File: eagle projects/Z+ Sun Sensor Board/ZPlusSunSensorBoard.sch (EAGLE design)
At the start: 50 parts, among them U2 ADS7841E_2K5, U4 LM20BIM7X_NOPB, U6 TLV9051IDCKR, U8 TLV9051IDCKR, U9 TLV9051IDCKR

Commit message: Rev B almost ready
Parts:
- removed A1: SUN_SENSOR_MOUNT, my_library:SUN_SENSOR_MOUNT
- removed C25, C28, C30: 4.7u, rcl:C-EUC0805
- removed C26, C29, C31: 0.1u, resistor:C-EUC0402
- removed C27, C32, C33: 0.022u, resistor:C-EUC0402
- removed J4, J5, J6: (no value), my_library:TRM_BLK_1X2
- removed R13, R19, R7: 3.74k, resistor:R-US_R0402
- removed R14, R8: 280R, resistor:R-US_R0402
- removed R15: 13.7k, resistor:R-US_R0402
- removed TP3, TP6, TP8: TESTPOINT, my_library:TESTPOINT
- removed U6, U9: TLV9051IDCKR, my_library:TLV9051IDCKR
- added C1, C17, C7: 4.7u, rcl:C-EUC0805
- added C18, C2, C8: 0.1u, resistor:C-EUC0402
- added C23, C3, C9: 0.022u, resistor:C-EUC0402
- added R10, R18: 13.7k, resistor:R-US_R0402
- added R11, R21, R5: 3.74k, resistor:R-US_R0402
- added R17: 280R, resistor:R-US_R0402
- added TP10, TP12, TP7: TESTPOINT, my_library:TESTPOINT
- added U$1: SSR_MOUNT_03, my_library:SSR_MOUNT_03
- added U1, U5: TSV991AILT, my_library:TSV991AILT
- R9: value 13.7k -> 280R
- U8: value TLV9051IDCKR -> TSV991AILT; device my_library:TLV9051IDCKR -> my_library:TSV991AILT
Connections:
- removed net N$13: R14.2, R15.1, U9.+
- removed net N$6: R1.2, R3.1, U6.+
- removed net N$9: R8.2, R9.1, U8.+
- new net N$11: C9.1, R11.1, U$1G$2.C2, U5.IN-
- new net N$14: R10.1, R9.2, U5.IN+
- new net N$20: R17.2, R18.1, U8.IN+
- net +3V3: now also C1.1, C17.1, C18.1, C2.1, C7.1, C8.1, R10.2, R18.2, U1.VCC, U5.VCC, U8.VCC; no longer C25.1, C26.1, C28.1, C29.1, C30.1, C31.1, R15.2, R9.2, U6.V+, U8.V+, U9.V+
- net 0_DEGREES: now also C3.2, R5.2, TP7.TP, U1.OUT; no longer C27.2, R7.2, TP3.TP, U6.OUT
- net 120_DEGREES: now also C9.2, R11.2, TP10.TP, U5.OUT; no longer C32.2, R13.2, TP6.TP, U8.OUT
- net 240_DEGREES: now also C23.2, R21.2, TP12.TP, U8.OUT; no longer C33.2, R19.2, TP8.TP, U9.OUT
- net GND: now also C1.2, C17.2, C18.2, C2.2, C7.2, C8.2, R17.1, R9.1, U$1G$2.A1, U$1G$2.A2, U$1G$2.A3, U1.VSS, U5.VSS, U8.VSS; no longer C25.2, C26.2, C28.2, C29.2, C30.2, C31.2, J4.1, J5.1, J6.1, R14.1, R8.1, U6.V-, U8.V-, U9.V-
- net N$12: now also C23.1, R21.1, U$1G$2.C3, U8.IN-; no longer C33.1, J4.2, R19.1, U9.-
- net N$3: now also C3.1, R5.1, U$1G$2.C1, U1.IN-; no longer C27.1, J6.2, R7.1, U6.-
- net N$8: now also R1.2, R3.1, U1.IN+; no longer C32.1, J5.2, R13.1, U8.-
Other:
- moved on the sheet: R1, R3, R9

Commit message: I thinks its done
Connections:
- net GND: now also H1.MOUNT, H2.MOUNT, H3.MOUNT, H4.MOUNT
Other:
- note added: "B"
- note removed: "A"
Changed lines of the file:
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@@
 <schematic xreflabel="%F%N" xrefpart="/%S.%C%R">
 <attributes>
-<attribute name="DESIGNER" value="T. Christison"/>
+<attribute name="DESIGNER" value="Thomas Christison"/>
+<attribute name="REV" value="B"/>
+<attribute name="REVIEWER" value="ADCS Electrical"/>
 </attributes>
 <variantdefs>
@@
 <part name="C12" library="rcl" library_urn="urn:adsk.eagle:library:334" deviceset="C-EU" device="C0402" package3d_urn="urn:adsk.eagle:package:23626/2" value="0.1u"/>
 <part name="SUPPLY24" library="supply2" library_urn="urn:adsk.eagle:library:372" deviceset="GND" device=""/>
-<part name="U2" library="my_library" library_urn="urn:adsk.eagle:library:22876504" deviceset="ADS7841E_2K5" device="" package3d_urn="urn:adsk.eagle:package:23087509/5"/>
+<part name="U2" library="my_library" library_urn="urn:adsk.eagle:library:22876504" deviceset="ADS7841E_2K5" device="" package3d_urn="urn:adsk.eagle:package:23087509/6"/>
 <part name="C14" library="resistor" library_urn="urn:adsk.eagle:library:348" deviceset="C-EU" device="C0402" package3d_urn="urn:adsk.eagle:package:23626/2" value="1u"/>
 <part name="C15" library="resistor" library_urn="urn:adsk.eagle:library:348" deviceset="C-EU" device="C0402" package3d_urn="urn:adsk.eagle:package:23626/2" value="0.1u"/>
@@
 <attribute name="DESIGNER" value=""/>
 <attribute name="REV#" value=""/>
+<attribute name="REVIEWER" value=""/>
 </part>
 <part name="R4" library="resistor" library_urn="urn:adsk.eagle:library:348" deviceset="R-US_" device="R0402" package3d_urn="urn:adsk.eagle:package:26058/2" value="5.1M"/>
 <part name="SUPPLY3" library="supply2" library_urn="urn:adsk.eagle:library:372" deviceset="GND" device=""/>
-<part name="U$1" library="my_library" library_urn="urn:adsk.eagle:library:22876504" deviceset="SSR_MOUNT_03" device="" package3d_urn="urn:adsk.eagle:package:29580098/1"/>
+<part name="U$1" library="my_library" library_urn="urn:adsk.eagle:library:22876504" deviceset="SSR_MOUNT_03" device="" package3d_urn="urn:adsk.eagle:package:29580098/1" override_package3d_urn="urn:adsk.eagle:package:30064049/2" override_package_urn="urn:adsk.eagle:footprint:29580096/1"/>
 <part name="SUPPLY6" library="supply2" library_urn="urn:adsk.eagle:library:372" deviceset="GND" device=""/>
 <part name="C1" library="rcl" library_urn="urn:adsk.eagle:library:334" deviceset="C-EU" device="C0805" package3d_urn="urn:adsk.eagle:package:23617/2" value="4.7u"/>
@@
 <part name="+3V11" library="supply1" library_urn="urn:adsk.eagle:library:371" deviceset="+3V3" device=""/>
 <part name="U8" library="my_library" library_urn="urn:adsk.eagle:library:22876504" deviceset="TSV991AILT" device="" package3d_urn="urn:adsk.eagle:package:24426275/2"/>
+<part name="SUPPLY13" library="supply2" library_urn="urn:adsk.eagle:library:372" deviceset="GND" device=""/>
+<part name="SUPPLY14" library="supply2" library_urn="urn:adsk.eagle:library:372" deviceset="GND" device=""/>
+<part name="SUPPLY15" library="supply2" library_urn="urn:adsk.eagle:library:372" deviceset="GND" device=""/>
+<part name="SUPPLY16" library="supply2" library_urn="urn:adsk.eagle:library:372" deviceset="GND" device=""/>
 </parts>
 <sheets>
 <sheet>
 <plain>
-<text x="262.128" y="7.112" size="2.54" layer="94">A</text>
+<text x="262.128" y="7.112" size="2.54" layer="94">B</text>
 <text x="190.754" y="11.43" size="2.54" layer="94">T. Christison</text>
 </plain>
@@
 <attribute name="REV#" x="261.62" y="7.62" size="2.54" layer="94"/>
 <attribute name="DESIGNER" x="196.85" y="11.43" size="2.54" layer="94"/>
+<attribute name="REVIEWER" x="196.85" y="6.35" size="2.54" layer="94"/>
 </instance>
 <instance part="R4" gate="G$1" x="233.68" y="93.98" smashed="yes" rot="R90">
@@
 <attribute name="NAME" x="99.06" y="53.34" size="1.778" layer="95"/>
 <attribute name="VALUE" x="99.06" y="50.8" size="1.778" layer="96"/>
+</instance>
+<instance part="SUPPLY13" gate="GND" x="10.16" y="7.62" smashed="yes">
+<attribute name="VALUE" x="8.255" y="4.445" size="1.778" layer="96"/>
+</instance>
+<instance part="SUPPLY14" gate="GND" x="48.26" y="7.62" smashed="yes">
+<attribute name="VALUE" x="46.355" y="4.445" size="1.778" layer="96"/>
+</instance>
+<instance part="SUPPLY15" gate="GND" x="88.9" y="7.62" smashed="yes">
+<attribute name="VALUE" x="86.995" y="4.445" size="1.778" layer="96"/>
+</instance>
+<instance part="SUPPLY16" gate="GND" x="129.54" y="7.62" smashed="yes">
+<attribute name="VALUE" x="127.635" y="4.445" size="1.778" layer="96"/>
 </instance>
 </instances>
@@
 <pinref part="SUPPLY36" gate="GND" pin="GND"/>
 <pinref part="U8" gate="G$1" pin="VSS"/>
+</segment>
+<segment>
+<pinref part="SUPPLY13" gate="GND" pin="GND"/>
+<wire x1="10.16" y1="10.16" x2="10.16" y2="12.7" width="0.1524" layer="91"/>
+<pinref part="H1" gate="G$1" pin="MOUNT"/>
+<wire x1="10.16" y1="12.7" x2="12.7" y2="12.7" width="0.1524" layer="91"/>
+</segment>
+<segment>
+<pinref part="SUPPLY14" gate="GND" pin="GND"/>
+<wire x1="48.26" y1="10.16" x2="48.26" y2="12.7" width="0.1524" layer="91"/>
+<pinref part="H2" gate="G$1" pin="MOUNT"/>
+<wire x1="48.26" y1="12.7" x2="50.8" y2="12.7" width="0.1524" layer="91"/>
+</segment>
+<segment>
+<pinref part="SUPPLY15" gate="GND" pin="GND"/>
+<wire x1="88.9" y1="10.16" x2="88.9" y2="12.7" width="0.1524" layer="91"/>
+<pinref part="H3" gate="G$1" pin="MOUNT"/>
+<wire x1="88.9" y1="12.7" x2="91.44" y2="12.7" width="0.1524" layer="91"/>
+</segment>
+<segment>
+<pinref part="SUPPLY16" gate="GND" pin="GND"/>
+<wire x1="129.54" y1="10.16" x2="129.54" y2="12.7" width="0.1524" layer="91"/>
+<pinref part="H4" gate="G$1" pin="MOUNT"/>
+<wire x1="129.54" y1="12.7" x2="132.08" y2="12.7" width="0.1524" layer="91"/>
 </segment>
 </net>
@@
 will not be understood (or retained) with this version.
 </note>
+<note version="9.4" severity="warning">
+Since Version 9.4, EAGLE supports the overriding of 3D packages
+in schematics and board files. Those overridden 3d packages
+will not be understood (or retained) with this version.
+</note>

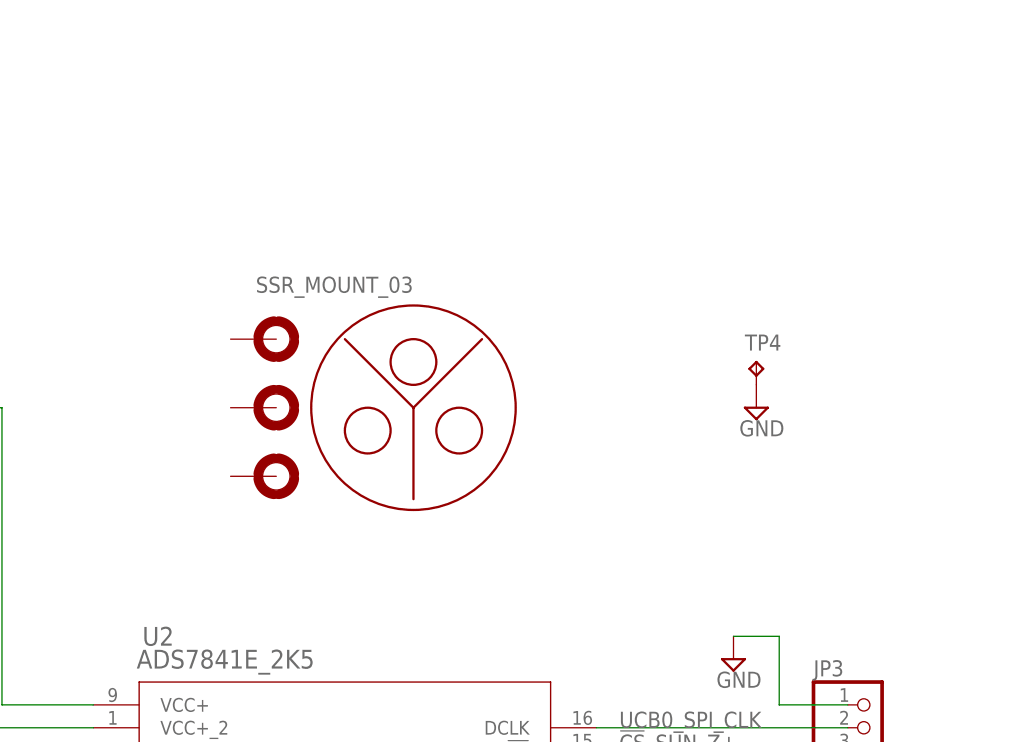
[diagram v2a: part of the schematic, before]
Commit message: Brandon added burn resistor components
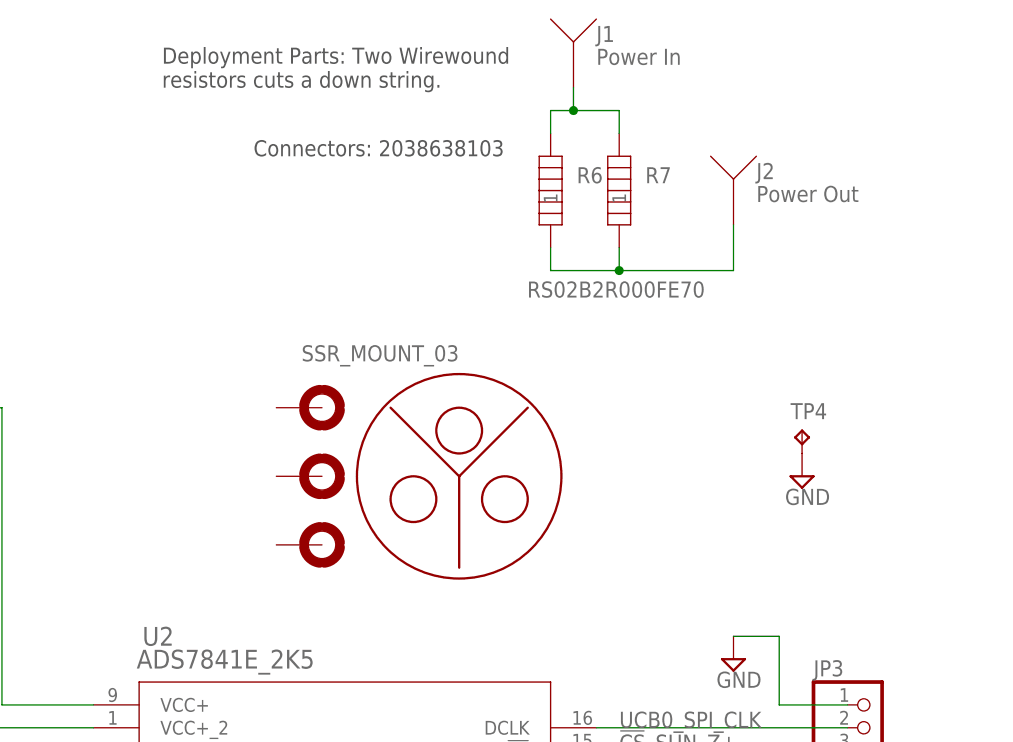
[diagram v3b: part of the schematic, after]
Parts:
- added J1: Power In, PDUv1:2038638103
- added J2: Power Out, PDUv1:2038638103
- added R6, R7: RS02B2R000FE70, Heating Element:RS02B2R000FE70
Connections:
- new net N$5: J1.P$1, R6.2, R7.2
- new net N$6: J2.P$1, R6.1, R7.1
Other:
- note added: "Connectors: 2038638103"
- note added: "Deployment Parts: Two Wirewound resistors cuts a down string."
- moved on the sheet: TP4

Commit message: dumb dumb fix dumb mistake
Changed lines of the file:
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@@
 <drawing>
 <settings>
-<setting alwaysvectorfont="no"/>
+<setting alwaysvectorfont="yes"/>
 <setting verticaltext="up"/>
 </settings>
@@
 <part name="C12" library="rcl" library_urn="urn:adsk.eagle:library:334" deviceset="C-EU" device="C0402" package3d_urn="urn:adsk.eagle:package:23626/2" value="0.1u"/>
 <part name="SUPPLY24" library="supply2" library_urn="urn:adsk.eagle:library:372" deviceset="GND" device=""/>
-<part name="U2" library="my_library" library_urn="urn:adsk.eagle:library:22876504" deviceset="ADS7841E_2K5" device="" package3d_urn="urn:adsk.eagle:package:23087509/8"/>
+<part name="U2" library="my_library" library_urn="urn:adsk.eagle:library:22876504" deviceset="ADS7841E_2K5" device="" package3d_urn="urn:adsk.eagle:package:23087509/6"/>
 <part name="C14" library="resistor" library_urn="urn:adsk.eagle:library:348" deviceset="C-EU" device="C0402" package3d_urn="urn:adsk.eagle:package:23626/2" value="1u"/>
 <part name="C15" library="resistor" library_urn="urn:adsk.eagle:library:348" deviceset="C-EU" device="C0402" package3d_urn="urn:adsk.eagle:package:23626/2" value="0.1u"/>
@@
 <part name="SUPPLY1" library="supply2" library_urn="urn:adsk.eagle:library:372" deviceset="GND" device=""/>
 <part name="SUPPLY2" library="supply2" library_urn="urn:adsk.eagle:library:372" deviceset="GND" device=""/>
-<part name="H1" library="my_library" library_urn="urn:adsk.eagle:library:22876504" deviceset="MOUNT-PAD-ROUND" device="" package3d_urn="urn:adsk.eagle:package:26858043/1"/>
-<part name="H2" library="my_library" library_urn="urn:adsk.eagle:library:22876504" deviceset="MOUNT-PAD-ROUND" device="" package3d_urn="urn:adsk.eagle:package:26858043/1"/>
-<part name="H3" library="my_library" library_urn="urn:adsk.eagle:library:22876504" deviceset="MOUNT-PAD-ROUND" device="" package3d_urn="urn:adsk.eagle:package:26858043/1"/>
-<part name="H4" library="my_library" library_urn="urn:adsk.eagle:library:22876504" deviceset="MOUNT-PAD-ROUND" device="" package3d_urn="urn:adsk.eagle:package:26858043/1"/>
+<part name="H1" library="my_library" library_urn="urn:adsk.eagle:library:22876504" deviceset="MOUNT-PAD-ROUND" device="" package3d_urn="urn:adsk.eagle:package:26858043/2"/>
+<part name="H2" library="my_library" library_urn="urn:adsk.eagle:library:22876504" deviceset="MOUNT-PAD-ROUND" device="" package3d_urn="urn:adsk.eagle:package:26858043/2"/>
+<part name="H3" library="my_library" library_urn="urn:adsk.eagle:library:22876504" deviceset="MOUNT-PAD-ROUND" device="" package3d_urn="urn:adsk.eagle:package:26858043/2"/>
+<part name="H4" library="my_library" library_urn="urn:adsk.eagle:library:22876504" deviceset="MOUNT-PAD-ROUND" device="" package3d_urn="urn:adsk.eagle:package:26858043/2"/>
 <part name="TP4" library="my_library" library_urn="urn:adsk.eagle:library:22876504" deviceset="TESTPOINT" device="" package3d_urn="urn:adsk.eagle:package:24605432/3"/>
 <part name="FRAME1" library="my_library" library_urn="urn:adsk.eagle:library:22876504" deviceset="TITLE_BLOCK_LETTER" device="">
@@
 <part name="R6" library="Heating Element" library_urn="urn:adsk.eagle:library:29300905" deviceset="RS02B2R000FE70" device="" package3d_urn="urn:adsk.eagle:package:29301001/2"/>
 <part name="R7" library="Heating Element" library_urn="urn:adsk.eagle:library:29300905" deviceset="RS02B2R000FE70" device="" package3d_urn="urn:adsk.eagle:package:29301001/2"/>
-<part name="J1" library="PDUv1" library_urn="urn:adsk.eagle:library:29653418" deviceset="2038638103" device="" package3d_urn="urn:adsk.eagle:package:30104253/3" value="Power In"/>
-<part name="J2" library="PDUv1" library_urn="urn:adsk.eagle:library:29653418" deviceset="2038638103" device="" package3d_urn="urn:adsk.eagle:package:30104253/3" value="Power Out"/>
+<part name="J1" library="PDUv1" library_urn="urn:adsk.eagle:library:29653418" deviceset="2038638103" device="" package3d_urn="urn:adsk.eagle:package:30104253/5" value="Power In"/>
+<part name="J2" library="PDUv1" library_urn="urn:adsk.eagle:library:29653418" deviceset="2038638103" device="" package3d_urn="urn:adsk.eagle:package:30104253/5" value="Power Out"/>
 </parts>
 <sheets>
@@
 </instance>
 <instance part="J2" gate="G$1" x="236.22" y="187.96" smashed="yes" rot="R90">
-<attribute name="NAME" x="238.76" y="187.96" size="1.778" layer="95"/>
-<attribute name="VALUE" x="238.76" y="185.42" size="1.778" layer="96"/>
+<attribute name="NAME" x="238.76" y="185.42" size="1.778" layer="95"/>
+<attribute name="VALUE" x="238.76" y="182.88" size="1.778" layer="96"/>
 </instance>
 </instances>
